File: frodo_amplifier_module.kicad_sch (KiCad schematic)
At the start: 40 parts, among them IC1 INA826AID, J1 JST-GH, J2 JST-GH, J3 Conn_01x02_Socket, J5 Conn_01x04_Socket, U2 MCP6001-OT, U3 MIC5504-3.3YM5, U4 ADC101C021CIMM

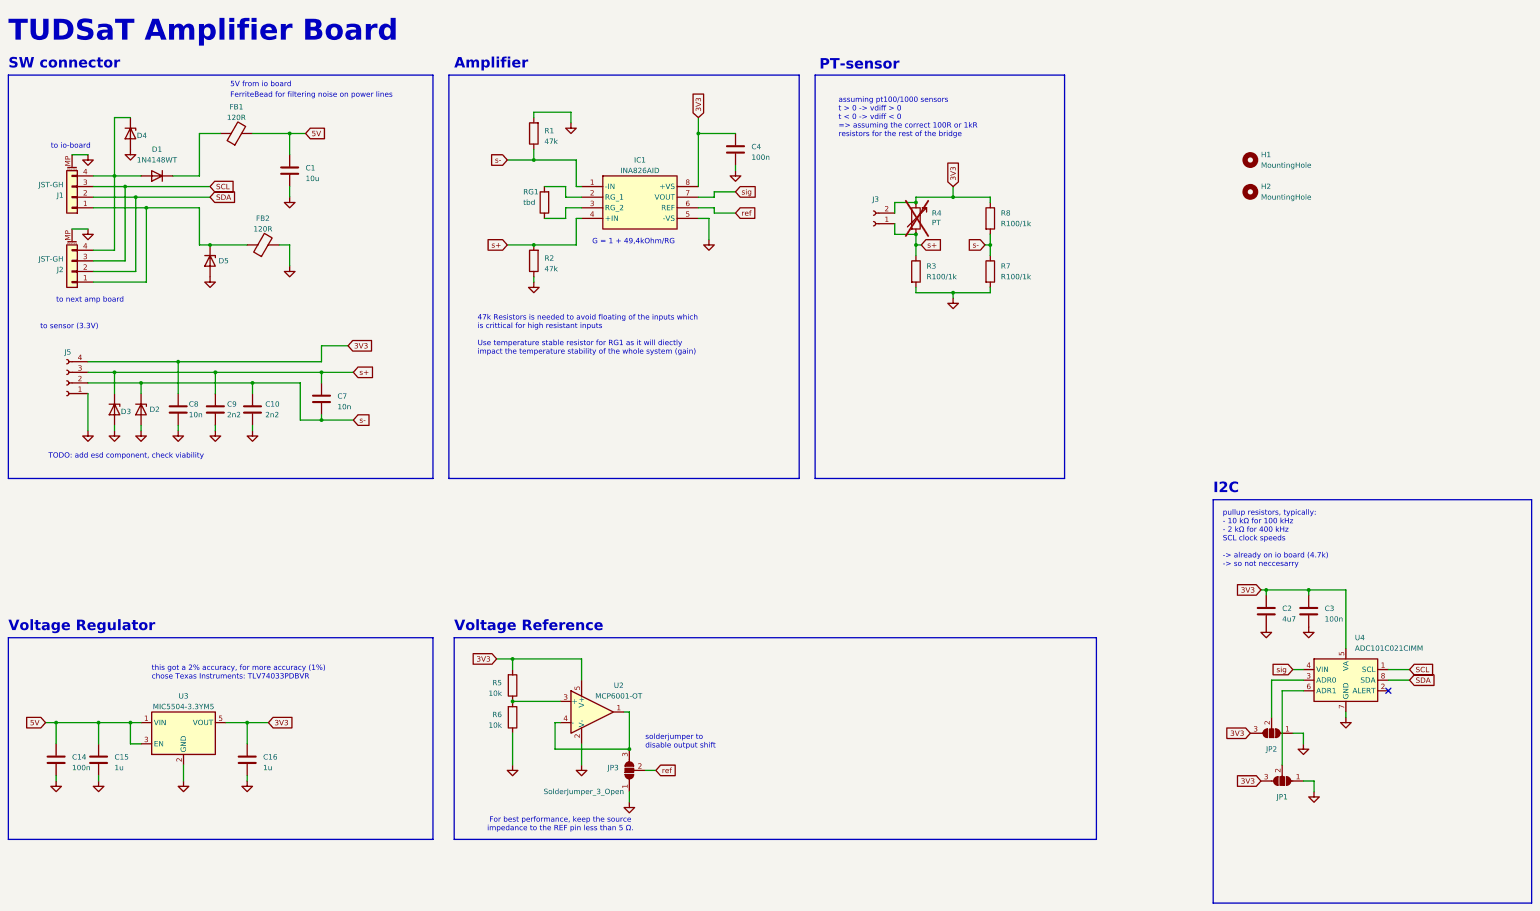
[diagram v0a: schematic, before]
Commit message: fixed design errors in amp board
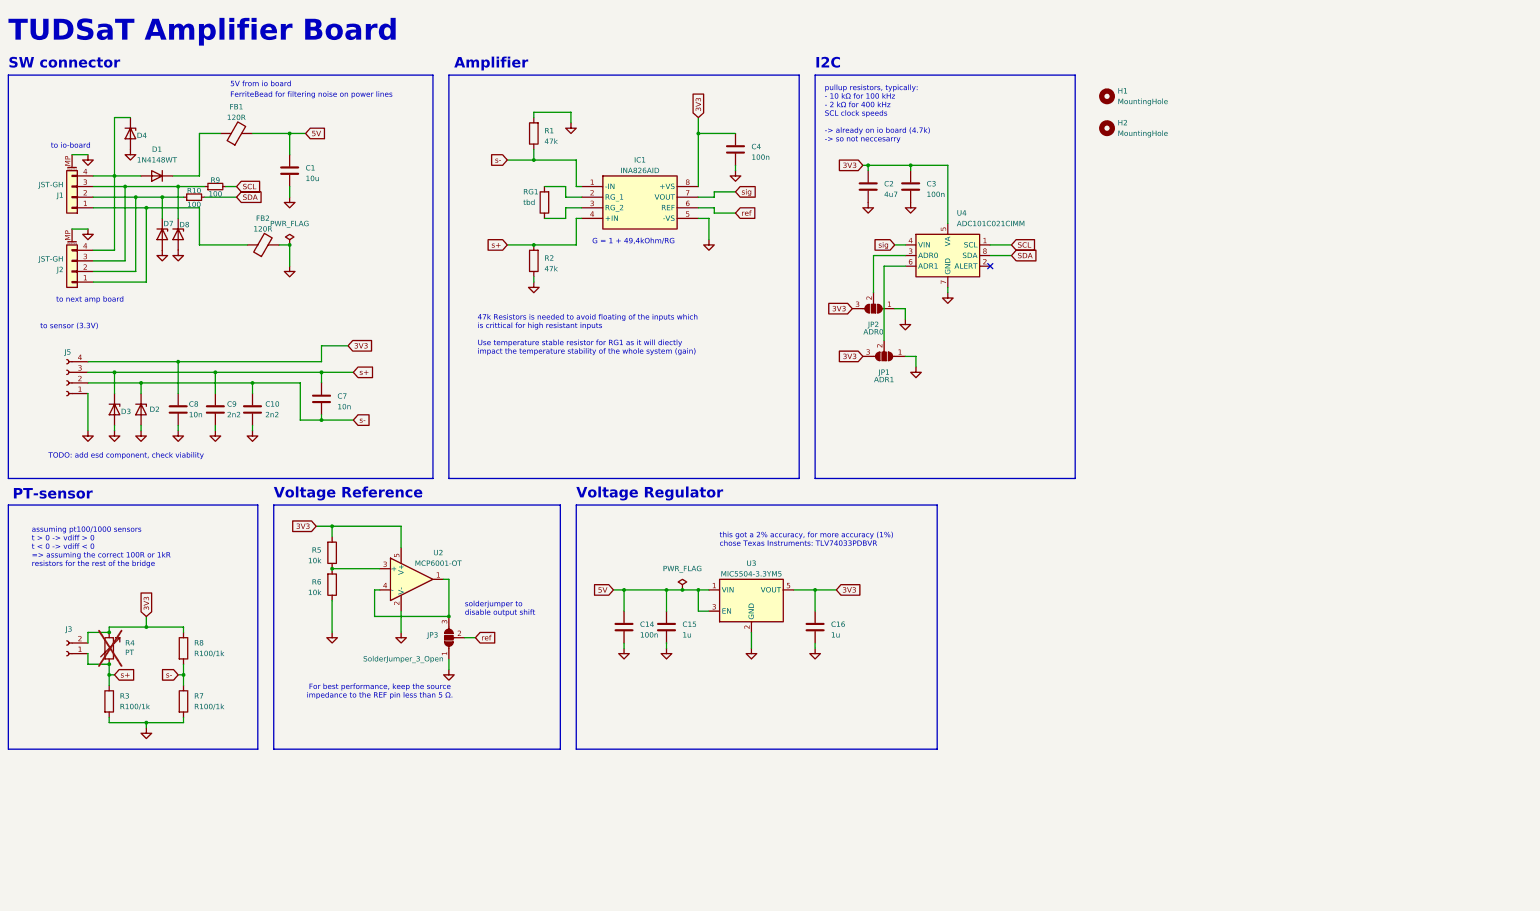
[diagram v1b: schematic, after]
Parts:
- removed D5: ESD5Zxx, Diode_SMD:D_SOD-523, symbol Diode:ESD5Zxx
- added D7, D8: ESD5Zxx, Diode_SMD:D_SOD-523, symbol Diode:ESD5Zxx
- added R10, R9: 100, Resistor_SMD:R_0402_1005Metric, symbol Device:R_Small
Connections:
- net GND: now also D7.2 (A), D8.2 (A)
- net SCL: now also R9.2; no longer J1.3 (Pin_3), J2.3 (Pin_3)
- net SDA: now also R10.2; no longer J1.2 (Pin_2), J2.2 (Pin_2)
- new net: D7.1 (K), J1.2 (Pin_2), J2.2 (Pin_2), R10.1
- new net: D8.1 (K), J1.3 (Pin_3), J2.3 (Pin_3), R9.1
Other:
- moved on the sheet: C14, C15, C16, C2, C3, H1, H2, J3, JP1, JP2, JP3, R3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
